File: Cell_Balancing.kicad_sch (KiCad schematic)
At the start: 27 parts, among them IC6 BQ7694204PFBR, J6 Conn_01x06, J7 Conn_01x04, Q10 MMBT5551LT1G

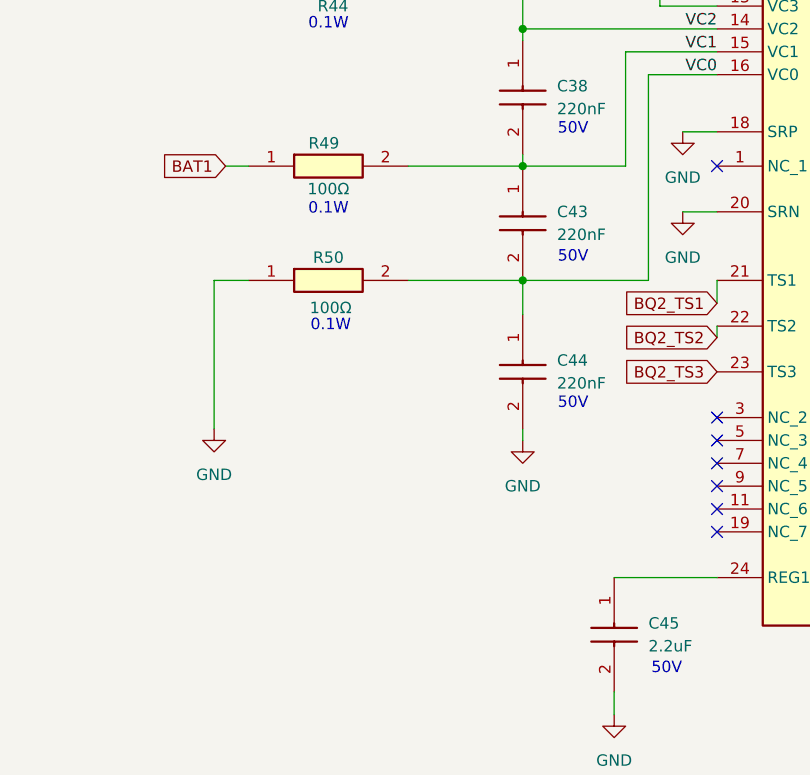
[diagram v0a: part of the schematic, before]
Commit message: Cap to GND fixed
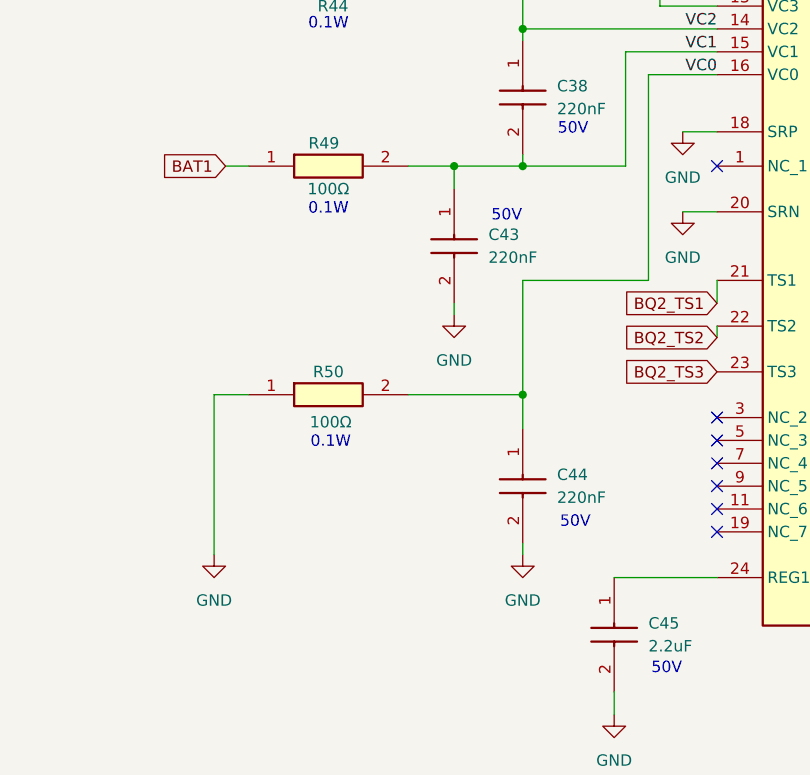
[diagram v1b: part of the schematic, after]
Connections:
- net GND: now also C43.2
- net VC0: no longer C43.2
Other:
- moved on the sheet: C43, C44, R50
